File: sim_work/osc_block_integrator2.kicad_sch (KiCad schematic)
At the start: 7 parts, among them U3 LM4562

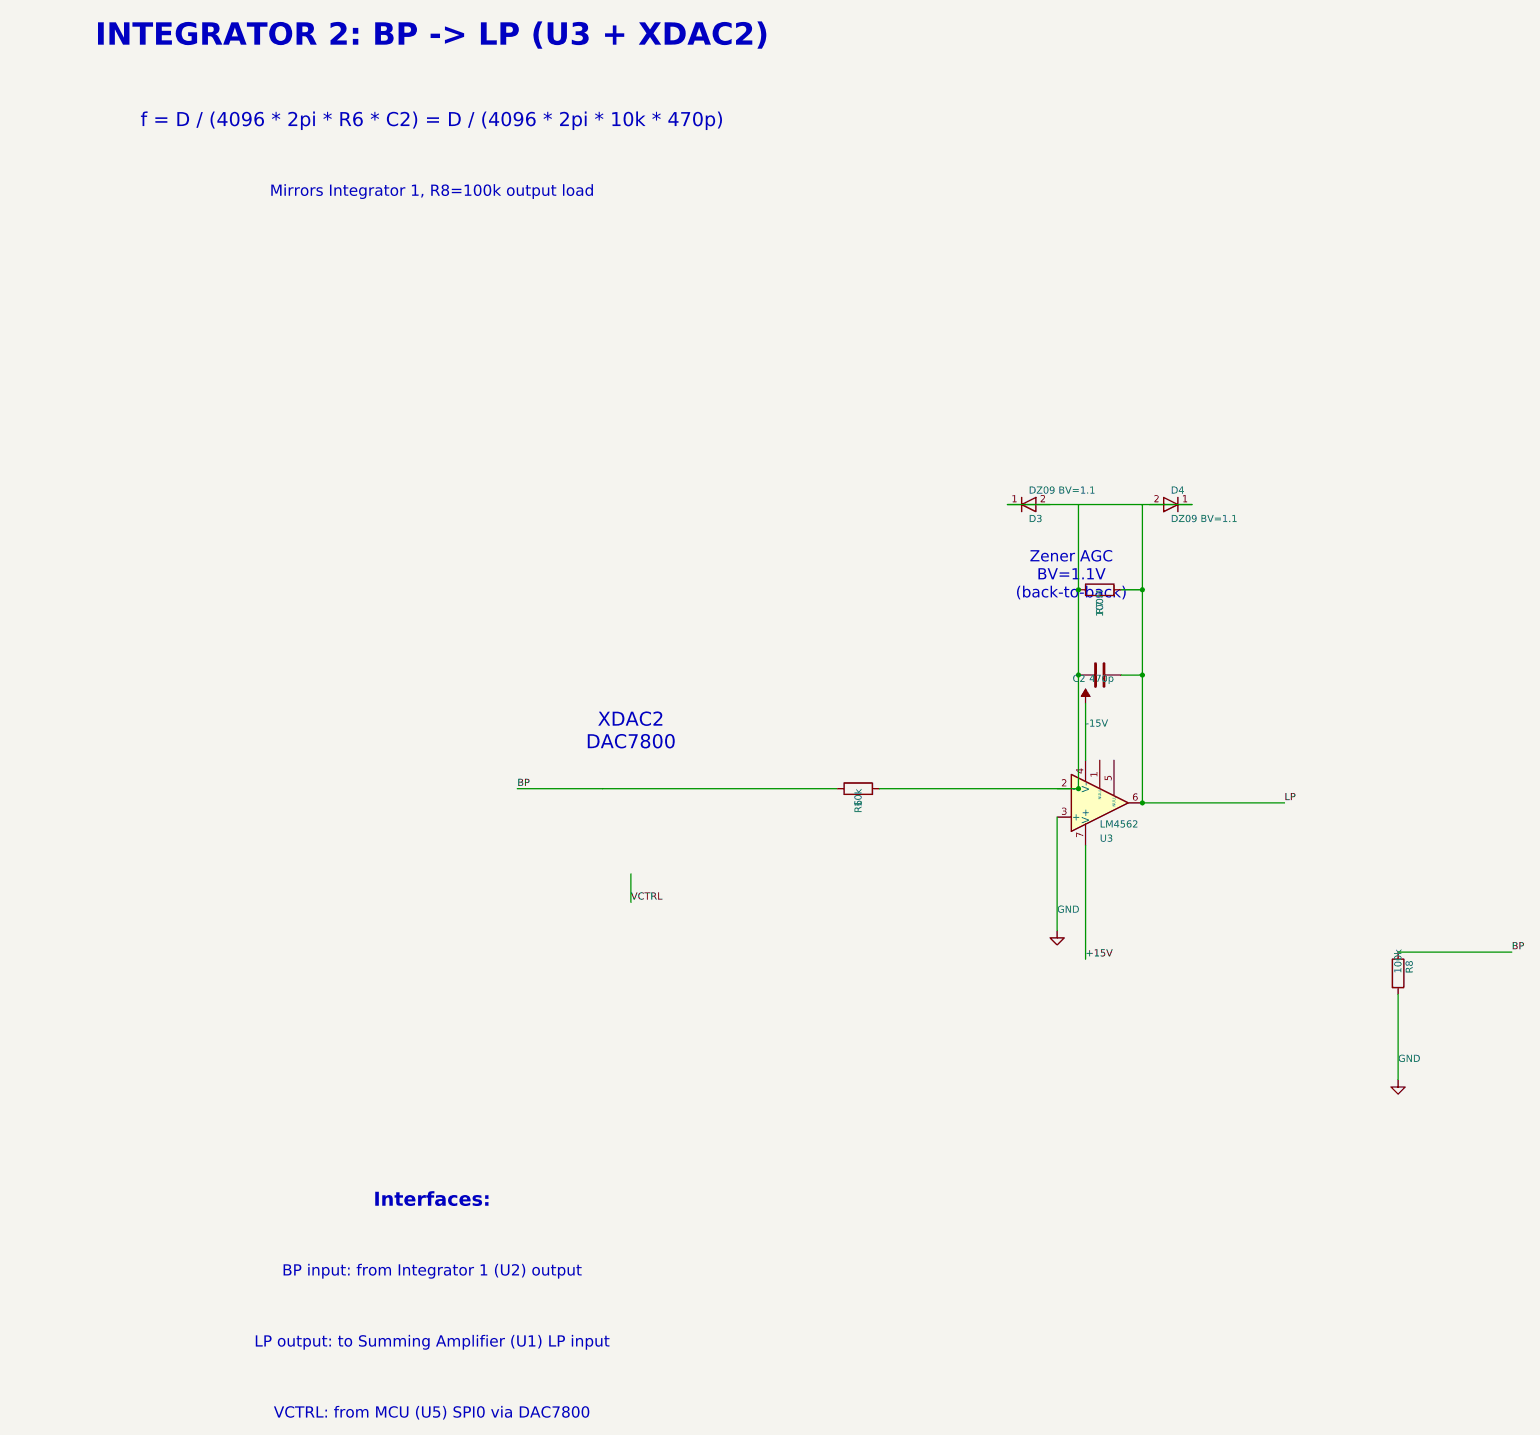
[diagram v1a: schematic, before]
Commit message: Fix schematic connections, add docs and repo portability
- Input filters: R rotation=90 (horizontal), ESD diode rotations fixed,
  junction dots at cathode-signal connection, wires to GND symbols
- Relay ladder: flyback diode rotation 270->90 (K top, A bottom)
- Electrometer/Mux TIA: 4 junction dots each at T-junctions
- AD636 RMS detector: proper IC box with pin labels replaces text-only
- Oscillator blocks: D_Zener symbol, L-shaped cathode routing
- TIA blocks: title/function annotations on all 5 blocks
- New: requirements.txt, docs/oscillator_guide.md
- D_Zener.kicad_sym added to bundled symbols/
- .gitignore updated for docs/ and requirements.txt
- README updated with pip install -r requirements.txt
- PROJECT.md session 9 changelog
- SimGUI builds clean (0 errors)

Co-Authored-By: Claude Opus 4.6 <noreply@anthropic.com>
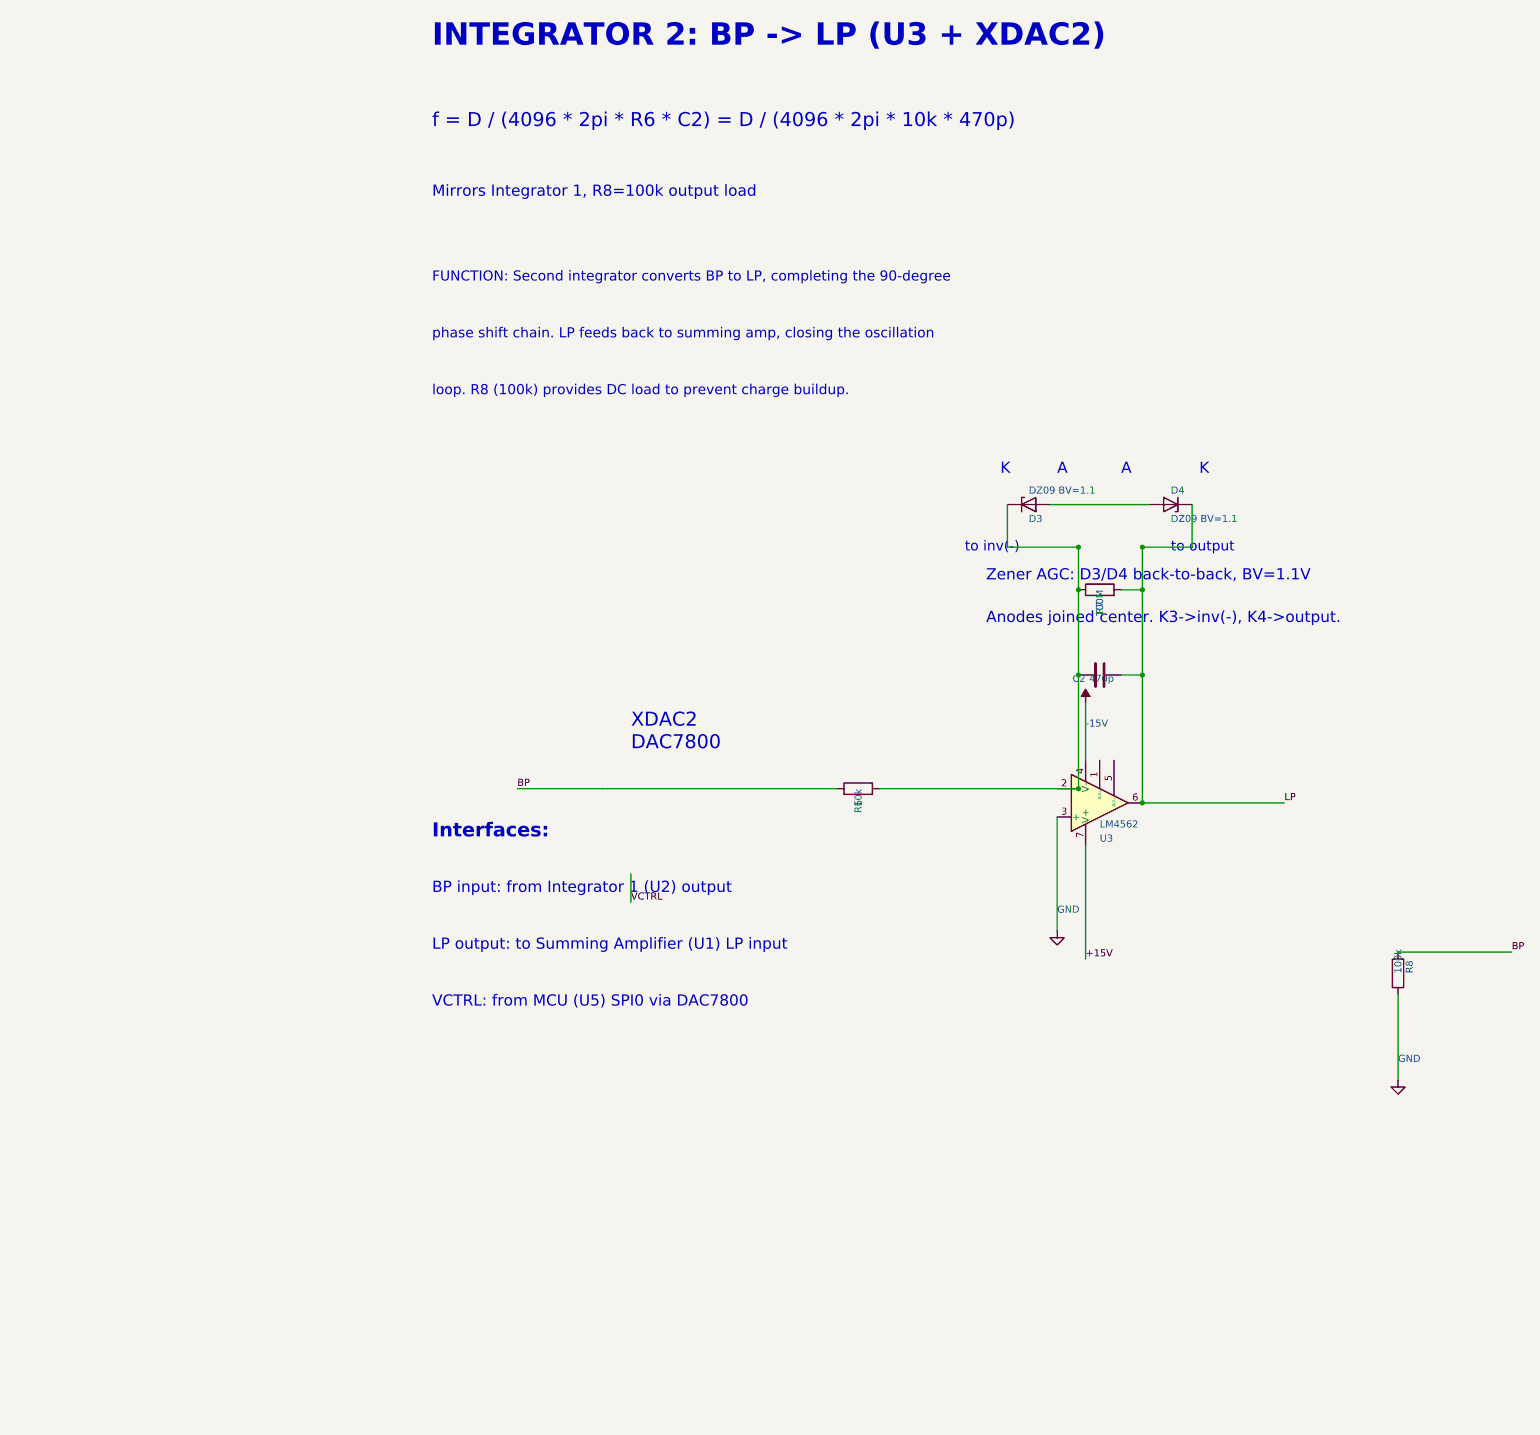
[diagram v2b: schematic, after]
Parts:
- removed D3, D4: DZ09 BV=1.1, symbol D:D
- added D3, D4: DZ09 BV=1.1, symbol D_Zener:D_Zener
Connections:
- net LP: now also D4.1 (K)
- net at C2.1, R6.2, R7.1: now also D3.1 (K)
- new net: D3.2 (A), D4.2 (A)
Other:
- note added: "A"
- note added: "Anodes joined center. K3->inv(-), K4->output."
- note added: "FUNCTION: Second integrator converts BP to LP, completing the 90-degree"
- note added: "K"
- note added: "Zener AGC: D3/D4 back-to-back, BV=1.1V"
- note added: "loop. R8 (100k) provides DC load to prevent charge buildup."
- note added: "phase shift chain. LP feeds back to summing amp, closing the oscillation"
- note added: "to inv(-)"
- note added: "to output"
- note removed: "Zener AGC BV=1.1V (back-to-back)"
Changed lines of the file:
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@@
 		(instances
 			(project "Oscillator - Integrator 2"
-				(path "/1adaa8b8-34fd-4b95-9d4f-627039dc5572"
+				(path "/f9c84676-b446-4d06-8fca-b90c590e8888"
 					(reference "U3")
 					(unit 1)
@@
 		(instances
 			(project "Oscillator - Integrator 2"
-				(path "/1adaa8b8-34fd-4b95-9d4f-627039dc5572"
+				(path "/f9c84676-b446-4d06-8fca-b90c590e8888"
 					(reference "R6")
 					(unit 1)
@@
 		(instances
 			(project "Oscillator - Integrator 2"
-				(path "/1adaa8b8-34fd-4b95-9d4f-627039dc5572"
+				(path "/f9c84676-b446-4d06-8fca-b90c590e8888"
 					(reference "C2")
 					(unit 1)
@@
 		(instances
 			(project "Oscillator - Integrator 2"
-				(path "/1adaa8b8-34fd-4b95-9d4f-627039dc5572"
+				(path "/f9c84676-b446-4d06-8fca-b90c590e8888"
 					(reference "R7")
 					(unit 1)
@@
 	)
 	(symbol
-		(lib_id "D:D")
+		(lib_id "D_Zener:D_Zener")
 		(at 127 99.06 0)
 		(unit 1)
@@
 		(instances
 			(project "Oscillator - Integrator 2"
-				(path "/1adaa8b8-34fd-4b95-9d4f-627039dc5572"
+				(path "/f9c84676-b446-4d06-8fca-b90c590e8888"
 					(reference "D3")
 					(unit 1)
@@
 	)
 	(symbol
-		(lib_id "D:D")
+		(lib_id "D_Zener:D_Zener")
 		(at 152.4 99.06 180)
 		(unit 1)
@@
 		(instances
 			(project "Oscillator - Integrator 2"
-				(path "/1adaa8b8-34fd-4b95-9d4f-627039dc5572"
+				(path "/f9c84676-b446-4d06-8fca-b90c590e8888"
 					(reference "D4")
 					(unit 1)
@@
 		(instances
 			(project "Oscillator - Integrator 2"
-				(path "/1adaa8b8-34fd-4b95-9d4f-627039dc5572"
+				(path "/f9c84676-b446-4d06-8fca-b90c590e8888"
 					(reference "#PWR001")
 					(unit 1)
@@
 		(instances
 			(project "Oscillator - Integrator 2"
-				(path "/1adaa8b8-34fd-4b95-9d4f-627039dc5572"
+				(path "/f9c84676-b446-4d06-8fca-b90c590e8888"
 					(reference "#PWR002")
 					(unit 1)
@@
 		(instances
 			(project "Oscillator - Integrator 2"
-				(path "/1adaa8b8-34fd-4b95-9d4f-627039dc5572"
+				(path "/f9c84676-b446-4d06-8fca-b90c590e8888"
 					(reference "R8")
 					(unit 1)
@@
 		(instances
 			(project "Oscillator - Integrator 2"
-				(path "/1adaa8b8-34fd-4b95-9d4f-627039dc5572"
+				(path "/f9c84676-b446-4d06-8fca-b90c590e8888"
 					(reference "#PWR003")
 					(unit 1)
@@
 	(wire
 		(pts
-			(xy 123.19 99.06) (xy 156.21 99.06)
-		)
-		(stroke
-			(width 0)
-			(type default)
-		)
-	)
-	(wire
-		(pts
-			(xy 135.89 99.06) (xy 135.89 114.3)
-		)
-		(stroke
-			(width 0)
-			(type default)
-		)
-	)
-	(wire
-		(pts
-			(xy 147.32 99.06) (xy 147.32 114.3)
+			(xy 130.81 99.06) (xy 148.59 99.06)
+		)
+		(stroke
+			(width 0)
+			(type default)
+		)
+	)
+	(wire
+		(pts
+			(xy 123.19 99.06) (xy 123.19 106.68)
+		)
+		(stroke
+			(width 0)
+			(type default)
+		)
+	)
+	(wire
+		(pts
+			(xy 123.19 106.68) (xy 135.89 106.68)
+		)
+		(stroke
+			(width 0)
+			(type default)
+		)
+	)
+	(wire
+		(pts
+			(xy 135.89 106.68) (xy 135.89 114.3)
+		)
+		(stroke
+			(width 0)
+			(type default)
+		)
+	)
+	(wire
+		(pts
+			(xy 156.21 99.06) (xy 156.21 106.68)
+		)
+		(stroke
+			(width 0)
+			(type default)
+		)
+	)
+	(wire
+		(pts
+			(xy 147.32 106.68) (xy 156.21 106.68)
+		)
+		(stroke
+			(width 0)
+			(type default)
+		)
+	)
+	(wire
+		(pts
+			(xy 147.32 106.68) (xy 147.32 114.3)
 		)
 		(stroke
@@
 	)
 	(junction
+		(at 135.89 106.68)
+		(diameter 0)
+		(color 0 0 0 0)
+	)
+	(junction
 		(at 135.89 114.3)
+		(diameter 0)
+		(color 0 0 0 0)
+	)
+	(junction
+		(at 147.32 106.68)
 		(diameter 0)
 		(color 0 0 0 0)
@@
 				(bold yes)
 			)
+			(justify left)
 		)
 	)
@@
 				(size 2.5 2.5)
 			)
+			(justify left)
 		)
 	)
@@
 				(size 2 2)
 			)
+			(justify left)
+		)
+	)
+	(text "FUNCTION: Second integrator converts BP to LP, completing the 90-degree"
+		(exclude_from_sim no)
+		(at 20.32 58.42 0.0000)
+		(effects
+			(font
+				(size 1.8 1.8)
+			)
+			(justify left)
+		)
+	)
+	(text "phase shift chain. LP feeds back to summing amp, closing the oscillation"
+		(exclude_from_sim no)
+		(at 20.32 68.58 0.0000)
+		(effects
+			(font
+				(size 1.8 1.8)
+			)
+			(justify left)
+		)
+	)
+	(text "loop. R8 (100k) provides DC load to prevent charge buildup."
+		(exclude_from_sim no)
+		(at 20.32 78.74 0.0000)
+		(effects
+			(font
+				(size 1.8 1.8)
+			)
+			(justify left)
 		)
 	)
@@
 				(size 2.5 2.5)
 			)
-		)
-	)
-	(text "Zener AGC\nBV=1.1V\n(back-to-back)"
-		(exclude_from_sim no)
-		(at 134.62 111.76 0.0000)
-		(effects
-			(font
-				(size 2 2)
-			)
+			(justify left)
+		)
+	)
+	(text "K"
+		(exclude_from_sim no)
+		(at 121.92 92.71 0.0000)
+		(effects
+			(font
+				(size 2 2)
+			)
+			(justify left)
+		)
+	)
+	(text "A"
+		(exclude_from_sim no)
+		(at 132.08 92.71 0.0000)
+		(effects
+			(font
+				(size 2 2)
+			)
+			(justify left)
+		)
+	)
+	(text "A"
+		(exclude_from_sim no)
+		(at 143.51 92.71 0.0000)
+		(effects
+			(font
+				(size 2 2)
+			)
+			(justify left)
+		)
+	)
+	(text "K"
+		(exclude_from_sim no)
+		(at 157.48 92.71 0.0000)
+		(effects
+			(font
+				(size 2 2)
+			)
+			(justify left)
+		)
+	)
+	(text "to inv(-)"
+		(exclude_from_sim no)
+		(at 115.57 106.68 0.0000)
+		(effects
+			(font
+				(size 1.8 1.8)
+			)
+			(justify left)
+		)
+	)
+	(text "to output"
+		(exclude_from_sim no)
+		(at 152.4 106.68 0.0000)
+		(effects
+			(font
+				(size 1.8 1.8)
+			)
+			(justify left)
+		)
+	)
+	(text "Zener AGC: D3/D4 back-to-back, BV=1.1V"
+		(exclude_from_sim no)
+		(at 119.38 111.76 0.0000)
+		(effects
+			(font
+				(size 2 2)
+			)
+			(justify left)
+		)
+	)
+	(text "Anodes joined center. K3->inv(-), K4->output."
+		(exclude_from_sim no)
+		(at 119.38 119.38 0.0000)
+		(effects
+			(font
+				(size 2 2)
+			)
+			(justify left)
 		)
 	)
 	(text "Interfaces:"
 		(exclude_from_sim no)
-		(at 20.32 223.52 0.0000)
+		(at 20.32 157.48 0.0000)
 		(effects
 			(font
@@
 				(bold yes)
 			)
+			(justify left)
 		)
 	)
 	(text "BP input: from Integrator 1 (U2) output"
 		(exclude_from_sim no)
-		(at 20.32 236.22 0.0000)
-		(effects
-			(font
-				(size 2 2)
-			)
+		(at 20.32 167.64 0.0000)
+		(effects
+			(font
+				(size 2 2)
+			)
+			(justify left)
 		)
 	)
 	(text "LP output: to Summing Amplifier (U1) LP input"
 		(exclude_from_sim no)
-		(at 20.32 248.92 0.0000)
-		(effects
-			(font
-				(size 2 2)
-			)
+		(at 20.32 177.8 0.0000)
+		(effects
+			(font
+				(size 2 2)
+			)
+			(justify left)
 		)
 	)
 	(text "VCTRL: from MCU (U5) SPI0 via DAC7800"
 		(exclude_from_sim no)
-		(at 20.32 261.62 0.0000)
-		(effects
-			(font
-				(size 2 2)
-			)
-		)
-	)
+		(at 20.32 187.96 0.0000)
+		(effects
+			(font
+				(size 2 2)
+			)
+			(justify left)
+		)
+	)

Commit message: Add comparison mode, fix SimGUI subprocess popups, DAC7800 IC boxes
- SimGUI: fix Python path detection (FindPython searches Python312/313/311)
- SimGUI: suppress console popup windows (CREATE_NO_WINDOW for subprocess)
- SimGUI: add Comparison project (MDAC vs Analog oscillator side-by-side)
- SimGUI: fix async wrapping (direct await instead of Task.Run)
- Pipeline: draw DAC7800 as proper IC box with pin labels (VREF/IOUT/VCTRL)
- Pipeline: fix electrometer_362 layout (spacing, junction dots at T-junctions)
- Pipeline: fix summing amp gain annotations (BP=-0.455, not -2.2)
- Pipeline: add analog_osc command for friend's SVF oscillator simulation
- Docs: comparison_guide.md, updated README and PROJECT tracker

Co-Authored-By: Claude Opus 4.6 <noreply@anthropic.com>
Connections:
- net +15V: now also U3.4 (V-); no longer U3.7 (V+)
- net -15V: now also U3.7 (V+); no longer U3.4 (V-)
- net BP: no longer R6.1
- net GND: now also U3.2 (-); no longer U3.3 (+)
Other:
- note added: "IOUT"
- note added: "VCTRL"
- note added: "VREF"
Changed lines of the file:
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@@
 		(lib_id "LM741:LM741")
 		(at 139.7 152.4 0)
-		(mirror x)
 		(unit 1)
 		(exclude_from_sim no)
@@
 		(instances
 			(project "Oscillator - Integrator 2"
-				(path "/f9c84676-b446-4d06-8fca-b90c590e8888"
+				(path "/34ba50e4-b613-4de1-b49d-4e1b31277ba2"
 					(reference "U3")
 					(unit 1)
@@
 		(instances
 			(project "Oscillator - Integrator 2"
-				(path "/f9c84676-b446-4d06-8fca-b90c590e8888"
+				(path "/34ba50e4-b613-4de1-b49d-4e1b31277ba2"
 					(reference "R6")
 					(unit 1)
@@
 		(instances
 			(project "Oscillator - Integrator 2"
-				(path "/f9c84676-b446-4d06-8fca-b90c590e8888"
+				(path "/34ba50e4-b613-4de1-b49d-4e1b31277ba2"
 					(reference "C2")
 					(unit 1)
@@
 		(instances
 			(project "Oscillator - Integrator 2"
-				(path "/f9c84676-b446-4d06-8fca-b90c590e8888"
+				(path "/34ba50e4-b613-4de1-b49d-4e1b31277ba2"
 					(reference "R7")
 					(unit 1)
@@
 		(instances
 			(project "Oscillator - Integrator 2"
-				(path "/f9c84676-b446-4d06-8fca-b90c590e8888"
+				(path "/34ba50e4-b613-4de1-b49d-4e1b31277ba2"
 					(reference "D3")
 					(unit 1)
@@
 		(instances
 			(project "Oscillator - Integrator 2"
-				(path "/f9c84676-b446-4d06-8fca-b90c590e8888"
+				(path "/34ba50e4-b613-4de1-b49d-4e1b31277ba2"
 					(reference "D4")
 					(unit 1)
@@
 		(instances
 			(project "Oscillator - Integrator 2"
-				(path "/f9c84676-b446-4d06-8fca-b90c590e8888"
+				(path "/34ba50e4-b613-4de1-b49d-4e1b31277ba2"
 					(reference "#PWR001")
 					(unit 1)
@@
 		(instances
 			(project "Oscillator - Integrator 2"
-				(path "/f9c84676-b446-4d06-8fca-b90c590e8888"
+				(path "/34ba50e4-b613-4de1-b49d-4e1b31277ba2"
 					(reference "#PWR002")
 					(unit 1)
@@
 		(instances
 			(project "Oscillator - Integrator 2"
-				(path "/f9c84676-b446-4d06-8fca-b90c590e8888"
+				(path "/34ba50e4-b613-4de1-b49d-4e1b31277ba2"
 					(reference "R8")
 					(unit 1)
@@
 		(instances
 			(project "Oscillator - Integrator 2"
-				(path "/f9c84676-b446-4d06-8fca-b90c590e8888"
+				(path "/34ba50e4-b613-4de1-b49d-4e1b31277ba2"
 					(reference "#PWR003")
 					(unit 1)
@@
 	(wire
 		(pts
-			(xy 35.56 149.86) (xy 50.8 149.86)
-		)
-		(stroke
-			(width 0)
-			(type default)
-		)
-	)
-	(wire
-		(pts
-			(xy 50.8 149.86) (xy 92.71 149.86)
-		)
-		(stroke
-			(width 0)
-			(type default)
-		)
-	)
-	(wire
-		(pts
-			(xy 55.88 170.18) (xy 55.88 165.1)
+			(xy 20.32 149.86) (xy 45.72 149.86)
+		)
+		(stroke
+			(width 0)
+			(type default)
+		)
+	)
+	(wire
+		(pts
+			(xy 76.2 149.86) (xy 92.71 149.86)
+		)
+		(stroke
+			(width 0)
+			(type default)
+		)
+	)
+	(wire
+		(pts
+			(xy 60.96 162.56) (xy 60.96 172.72)
 		)
 		(stroke
@@
 	)
 	(label "BP"
-		(at 35.56 149.86 0)
+		(at 20.32 149.86 0)
 		(effects
 			(font
@@
 	)
 	(label "VCTRL"
-		(at 55.88 170.18 0)
+		(at 60.96 172.72 0)
 		(effects
 			(font
@@
 		)
 	)
+	(rectangle
+		(start 45.72 137.16)
+		(end 76.2 162.56)
+		(stroke
+			(width 0.3)
+			(type solid)
+		)
+		(fill
+			(type none)
+		)
+	)
 	(text "INTEGRATOR 2: BP -> LP (U3 + XDAC2)"
 		(exclude_from_sim no)
@@
 	(text "XDAC2\nDAC7800"
 		(exclude_from_sim no)
-		(at 55.88 139.7 0.0000)
-		(effects
-			(font
-				(size 2.5 2.5)
-			)
-			(justify left)
+		(at 50.8 142.24 0.0000)
+		(effects
+			(font
+				(size 2 2)
+				(bold yes)
+			)
+			(justify left)
+		)
+	)
+	(text "VREF"
+		(exclude_from_sim no)
+		(at 48.26 152.4 0.0000)
+		(effects
+			(font
+				(size 1.5 1.5)
+			)
+			(justify left)
+		)
+	)
+	(text "IOUT"
+		(exclude_from_sim no)
+		(at 63.5 152.4 0.0000)
+		(effects
+			(font
+				(size 1.5 1.5)
+			)
+			(justify left)
+		)
+	)
+	(text "VCTRL"
+		(exclude_from_sim no)
+		(at 53.34 154.94 0.0000)
+		(effects
+			(font
+				(size 1.5 1.5)
+			)
+			(justify left)
